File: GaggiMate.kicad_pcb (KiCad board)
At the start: 4 copper layers, 76 x 90.1 mm, 59 parts, among them J1 Analog sensors, J10 K-Type probe, J11 Pressure Sensor, J12 Analog sensors, J13 K-Type probe, J14 Relays, J15 HV In, J2 Pressure Sensor, J3 BTNS, J5 Debug Pins, J6 Conn_02x08_Odd_Even, J7 Relays, J8 Heater SSR, J9 HV In, P1 USB_C_Plug_USB2.0, U1 ADS1115IDGS, U2 USBLC6-2SC6, U3 ESP32-S3-WROOM-1, U4 MAX31855KASA, U5 AMS1117-3.3, U6 AQH2223A, U7 AQH2223A

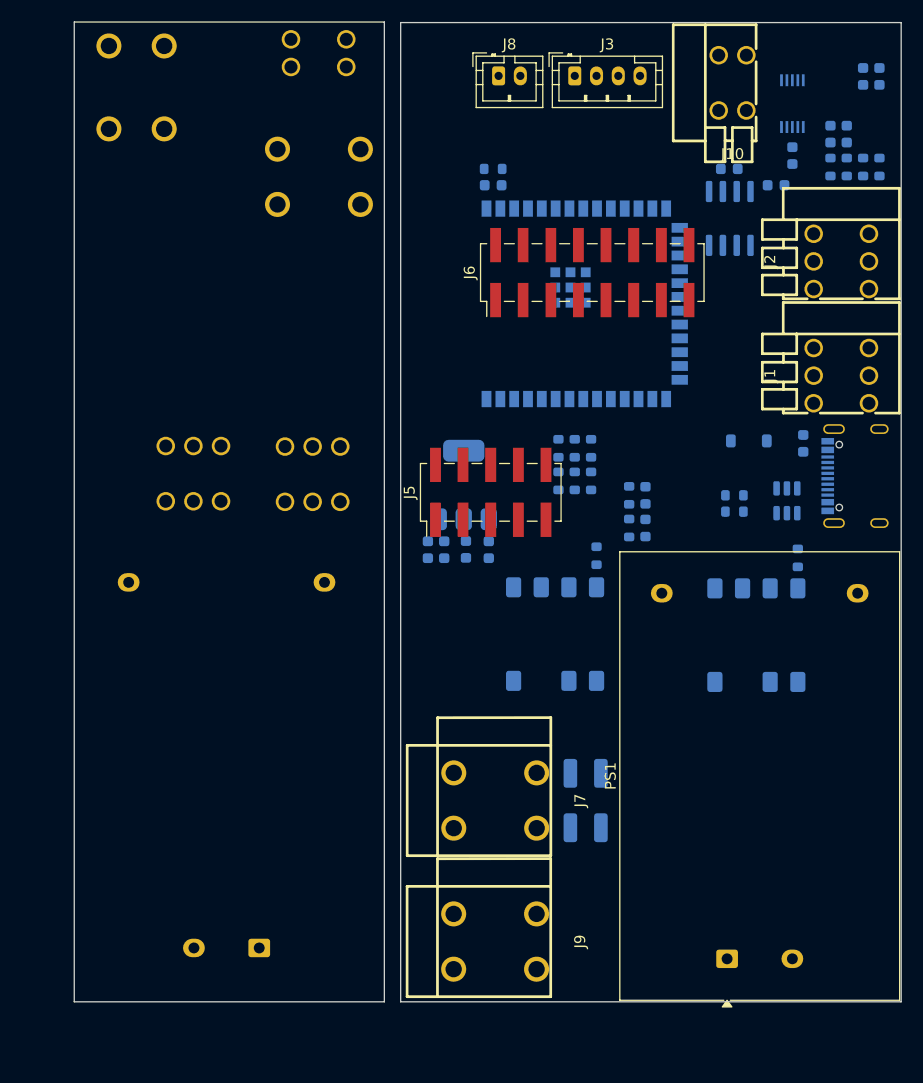
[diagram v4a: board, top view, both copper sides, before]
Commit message: geographical referencing instead
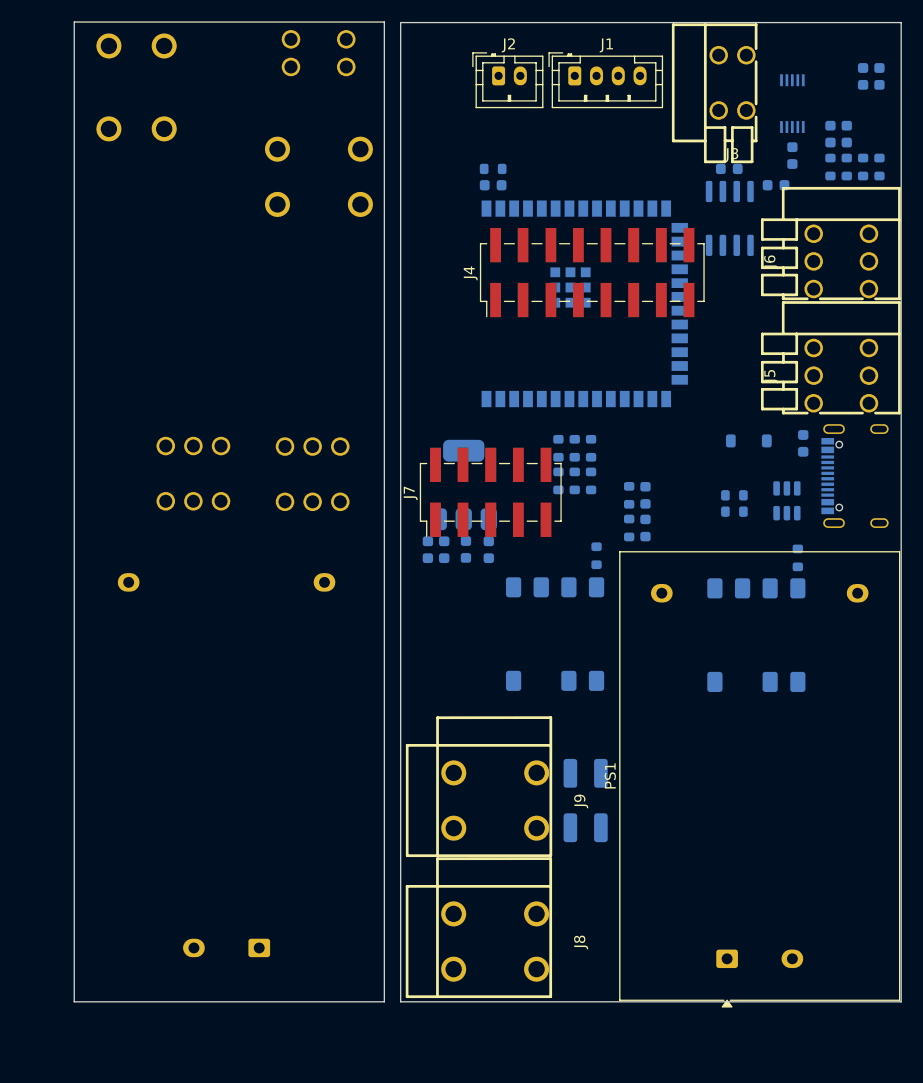
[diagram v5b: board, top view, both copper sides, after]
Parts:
- renumbered C1 to C0, C11 to C1, C13 to C10, C8 to C11, C9 to C12, C6 to C2, C5 to C3, C2 to C5, C10 to C6, C3 to C7, C7 to C8, C12 to C9, D1 to D0, D2 to D1, D3 to D2, J3 to J1, J13 to J10, J15 to J11, J14 to J12, J12 to J13, J11 to J14, J8 to J2, J10 to J3, J6 to J4, J1 to J5, J2 to J6, J5 to J7, J9 to J8, J7 to J9, P1 to P0, R7 to R0, R15 to R1, R12 to R10, R8 to R11, R11 to R12, R2 to R14, R4 to R15, R14 to R2, R9 to R3, R1 to R4, R17 to R7, R10 to R8, R3 to R9, RV1 to RV0, RV2 to RV1, U1 to U0, U4 to U1, U3 to U2, U7 to U3, U2 to U4, U6 to U5, U5 to U6

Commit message: attempt some routing
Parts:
- moved RV0 1.45 mm to (127.0, 117.6), turned to 90 degrees
- moved RV1 1.45 mm to (127.0, 125.5), turned to -90 degrees
- moved PS1 0.78 mm to (139.5, 135.5)
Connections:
- U3 pad 6: HV_NC -> unconnected-(U3-Pad6)
- U5 pad 6: HV_NC -> unconnected-(U5-Pad6)
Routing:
- net HV_L: track 0.00 -> 100.3 mm, vias 0 -> 4
- net HV_PUMP: track 0.00 -> 25.9 mm, vias 0 -> 2
- net HV_N: track 0.00 -> 24.9 mm
- net HV_VALVE: track 0.00 -> 15.5 mm, vias 0 -> 2

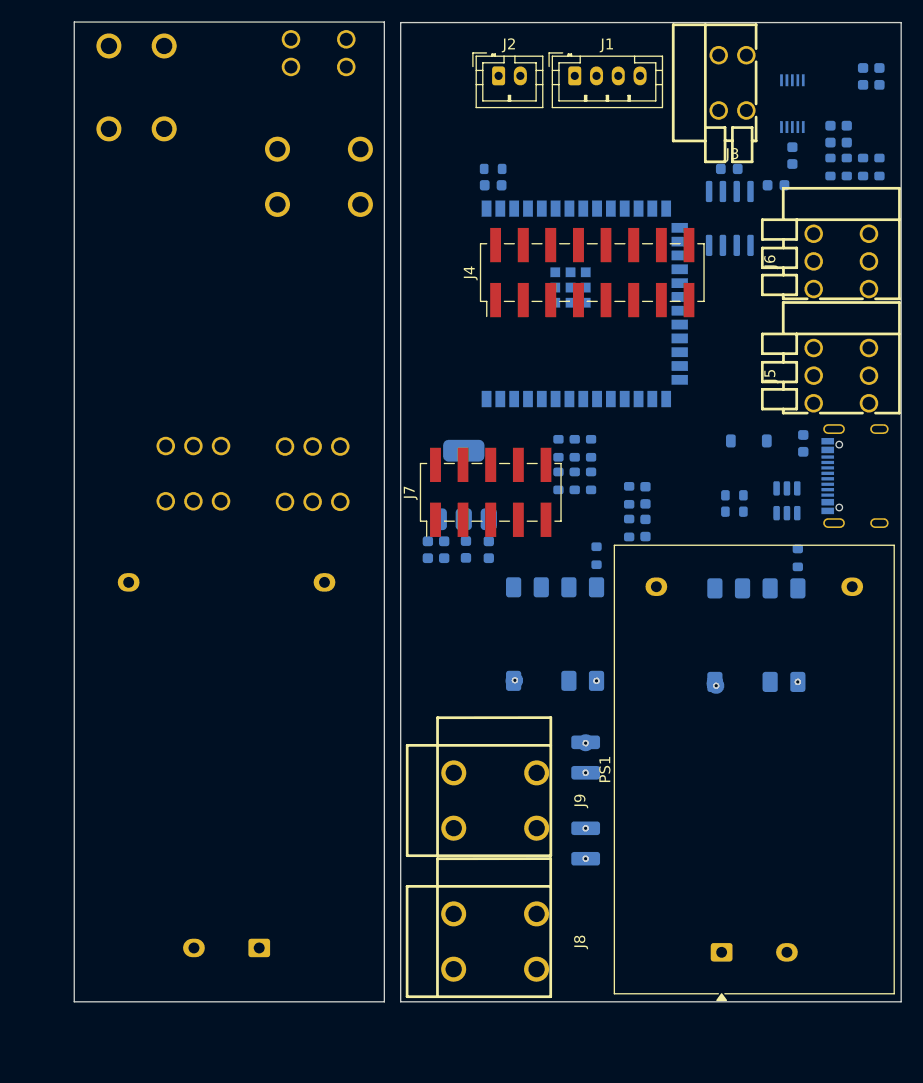
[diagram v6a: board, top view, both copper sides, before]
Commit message: update analog filters and started some HV traces
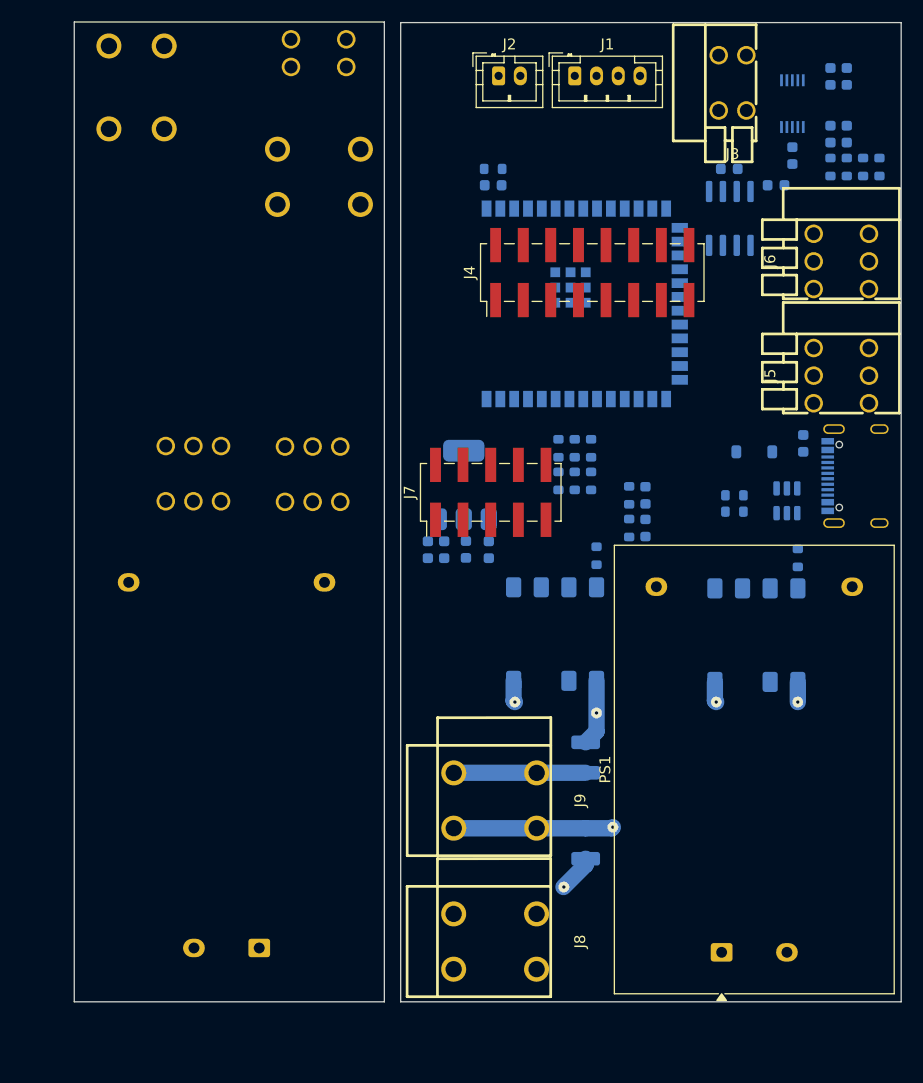
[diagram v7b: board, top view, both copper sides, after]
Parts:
- moved C2 3.00 mm to (151.0, 55.0)
- moved C3 3.00 mm to (149.5, 55.0)
- moved D0 1.12 mm to (142.5, 89.5)
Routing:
- net HV_L: track 100.3 -> 83.0 mm, vias 4 -> 3
- net HV_N: track 24.9 -> 35.4 mm
- net HV_PUMP: track 25.9 -> 33.5 mm
- net HV_VALVE: track 15.5 -> 21.5 mm, vias 2 -> 1

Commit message: more routing and and programming buttons
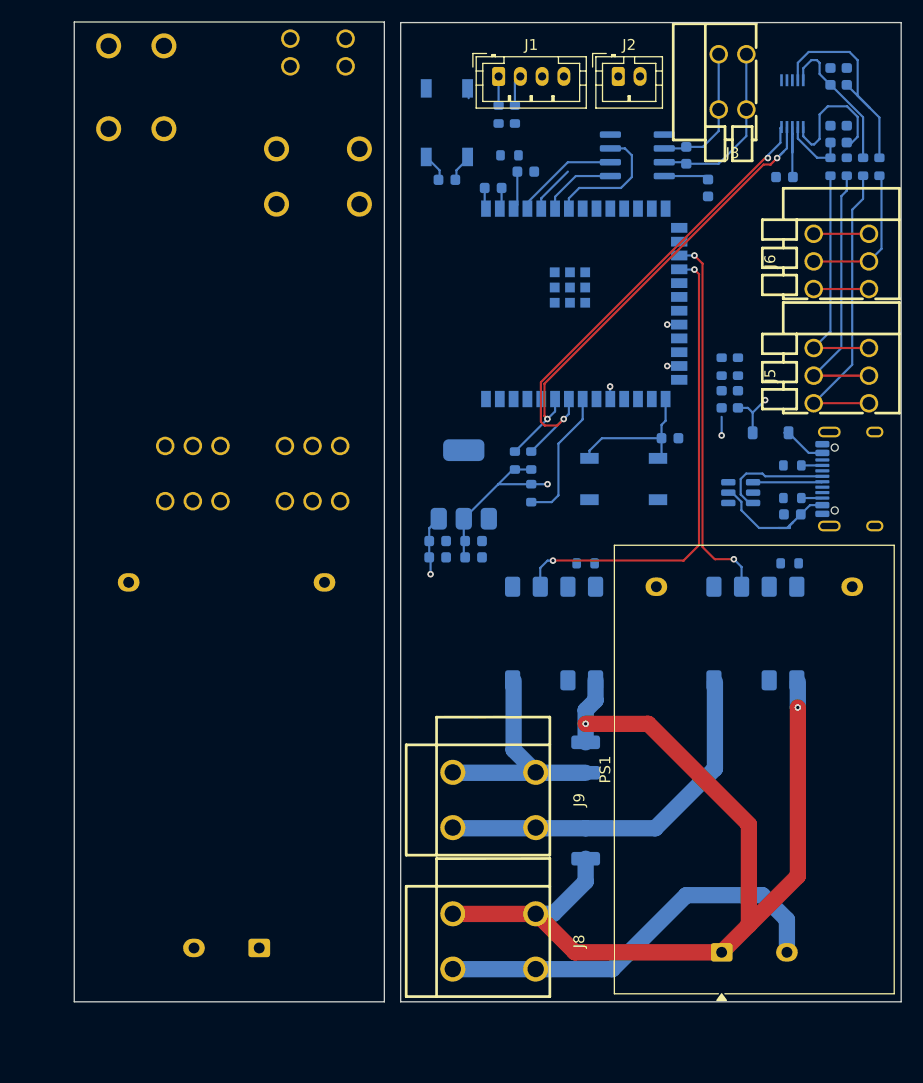
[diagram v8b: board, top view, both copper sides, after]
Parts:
- removed J4: Conn_02x08_Odd_Even, Connector_PinHeader_2.54mm:PinHeader_2x08_P2.54mm_Vertical_SMD
- removed J7: Debug Pins, Connector_PinHeader_2.54mm:PinHeader_2x05_P2.54mm_Vertical_SMD
- removed R4: 10k, Resistor_SMD:R_0603_1608Metric
- added C13: 0.1uF, Capacitor_SMD:C_0603_1608Metric, B.Cu at (114.2, 64.5)
- added C14: 0.1uF, Capacitor_SMD:C_0603_1608Metric, B.Cu at (134.8, 88.2)
- added C15: 10uF, Capacitor_SMD:C_0603_1608Metric, B.Cu at (121.5, 63.8)
- added SW1: SW_Push, Button_Switch_SMD:SW_SPST_TL3342, B.Cu at (114.2, 59.2)
- added SW2: SW_Push, Button_Switch_SMD:SW_SPST_TL3342, B.Cu at (130.5, 92.0)
- C2, C3, C4, C5: value 22nF -> 100nF
- P0: footprint Connector_USB:USB_C_Receptacle_Palconn_UTC16-G -> Connector_USB:USB_C_Receptacle_HCTL_HC-TYPE-C-16P-01A
- R0, R1, R2, R3: value 845 -> 1k
- moved R9 34.7 mm to (119.0, 58.5), turned to 90 degrees
- moved R15 33.9 mm to (120.5, 58.5), turned to -90 degrees
- moved R14 28.0 mm to (120.0, 62.2), turned to 0 degrees
- moved R8 17.9 mm to (141.0, 81.7), turned to 90 degrees
- moved D1 14.6 mm to (141.0, 84.7)
- moved R13 14.6 mm to (139.5, 81.7)
- moved D2 11.3 mm to (139.5, 84.7), turned to -90 degrees
- moved J2 11.0 mm to (130.0, 55.0)
- moved U1 10.3 mm to (131.8, 62.2), turned to 180 degrees
- moved J1 7.00 mm to (119.0, 55.0)
- moved C7 6.60 mm to (146.0, 95.2), turned to 180 degrees
- moved C6 6.25 mm to (138.2, 65.2), turned to -90 degrees
- moved R5 5.99 mm to (146.0, 90.8)
- moved R6 5.47 mm to (146.0, 93.8)
- moved U4 4.32 mm to (141.2, 93.2), turned to 180 degrees
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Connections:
- net /K-Probe T+ renamed T+
- net /K-Probe T- renamed T-
- J5 pad 1: AIN3 -> AIN1
- J5 pad 3: AIN1 -> AIN3
- R14 pad 1: BOOT -> 3.3V
- R14 pad 2: 3.3V -> EN
- U2 pad 36: /A1 -> U0RXD
- U2 pad 37: /A0 -> U0TXD
- U2 pad 8: unconnected-(U2-GPIO15/U0RTS/ADC2_CH4/XTAL_32K_P-Pad8) -> U0RTS
- U2 pad 9: unconnected-(U2-GPIO16/U0CTS/ADC2_CH5/XTAL_32K_N-Pad9) -> U0CTS
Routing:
- net 5V: track 0.00 -> 87.8 mm, vias 0 -> 2
- net 3.3V: track 0.00 -> 48.6 mm, vias 0 -> 2
- net I2C_SCL: track 0.00 -> 45.1 mm, vias 0 -> 2
- net VALVE: track 0.00 -> 44.1 mm, vias 0 -> 2
- net I2C_SDA: track 0.00 -> 43.7 mm, vias 0 -> 2
- net PUMP: track 0.00 -> 34.7 mm, vias 0 -> 2
- net AIN1: track 0.00 -> 27.9 mm
- net AIN2: track 0.00 -> 24.7 mm
- net AIN3: track 0.00 -> 21.6 mm
- net Net-(U0-AIN0): track 0.00 -> 20.6 mm
- net Net-(D0-A): track 0.00 -> 17.2 mm
- net T+: track 0.00 -> 16.2 mm
- net BOOT: track 0.00 -> 13.5 mm
- net PRESSURE: track 0.00 -> 13.5 mm
- net Net-(U0-AIN1): track 0.00 -> 13.4 mm
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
